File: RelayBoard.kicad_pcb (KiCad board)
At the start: 2 copper layers, 162 parts, among them P1 HE10-32, P2 CONN_2, Q1 NPN, Q10 NPN, Q11 NPN, Q12 NPN, Q13 NPN, Q14 NPN, Q15 NPN, Q16 NPN, Q17 NPN, Q18 NPN, Q19 NPN, Q2 NPN, Q20 NPN, Q21 NPN, Q22 NPN, Q23 NPN, Q24 NPN, Q25 NPN, Q26 NPN, Q27 NPN, Q28 NPN, Q29 NPN, Q3 NPN, Q30 NPN, Q31 NPN, Q32 NPN, Q4 NPN, Q5 NPN, Q6 NPN, Q7 NPN, Q8 NPN, Q9 NPN

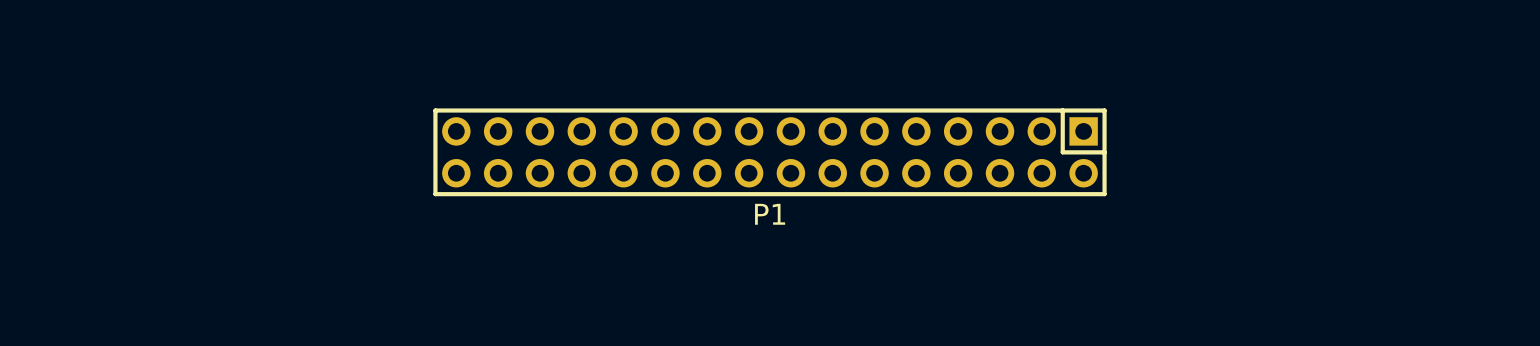
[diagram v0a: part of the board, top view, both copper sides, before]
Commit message: Changed the footprint of primary input header from 2x16 to 1x32 Due to routing concerns
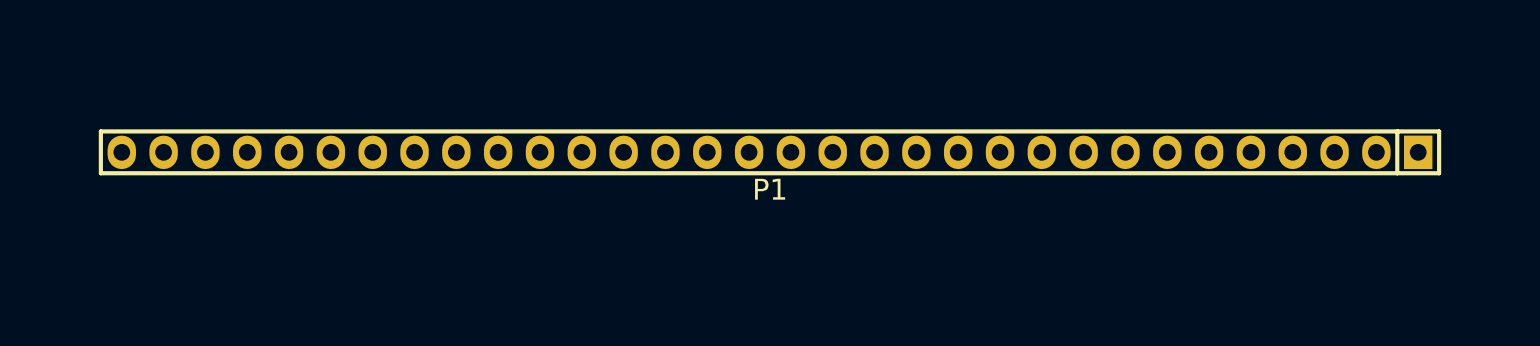
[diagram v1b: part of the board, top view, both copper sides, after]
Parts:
- P1: footprint Pin_Headers:Pin_Header_Straight_2x16 -> Pin_Headers:Pin_Header_Straight_1x32
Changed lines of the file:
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@@
     (links 320)
     (no_connects 320)
-    (area 30.48 19.05 344.17 180.34)
+    (area 30.48 20.01 343.994286 180.27)
     (thickness 1.6)
     (drawings 3)
@@
     )
   )
-  (module Pin_Headers:Pin_Header_Straight_2x16 (layer F.Cu)
+  (module Pin_Headers:Pin_Header_Straight_1x32 (layer F.Cu)
     (at 219.71 100.33 180)
     (descr "1 pin")
     (tags "CONN DEV")
-    (fp_text reference P1 (at 0 -3.81 180) (layer F.SilkS)
+    (fp_text reference P1 (at 0 -2.286 180) (layer F.SilkS)
       (effects (font (size 1.27 1.27) (thickness 0.2032)))
     )
@@
       (effects (font (size 1.27 1.27) (thickness 0.2032)))
     )
-    (fp_line (start 20.32 -2.54) (end -20.32 -2.54) (layer F.SilkS) (width 0.254))
-    (fp_line (start -17.78 2.54) (end 20.32 2.54) (layer F.SilkS) (width 0.254))
-    (fp_line (start 20.32 -2.54) (end 20.32 2.54) (layer F.SilkS) (width 0.254))
-    (fp_line (start -20.32 -2.54) (end -20.32 0) (layer F.SilkS) (width 0.254))
-    (fp_line (start -20.32 2.54) (end -17.78 2.54) (layer F.SilkS) (width 0.254))
-    (fp_line (start -20.32 0) (end -17.78 0) (layer F.SilkS) (width 0.254))
-    (fp_line (start -17.78 0) (end -17.78 2.54) (layer F.SilkS) (width 0.254))
-    (fp_line (start -20.32 2.54) (end -20.32 0) (layer F.SilkS) (width 0.254))
-    (pad 1 thru_hole rect (at -19.05 1.27 180) (size 1.7272 1.7272) (drill 1.016) (layers *.Cu *.Mask F.SilkS)
+    (fp_line (start -38.1 1.27) (end 40.64 1.27) (layer F.SilkS) (width 0.254))
+    (fp_line (start 40.64 1.27) (end 40.64 -1.27) (layer F.SilkS) (width 0.254))
+    (fp_line (start 40.64 -1.27) (end -38.1 -1.27) (layer F.SilkS) (width 0.254))
+    (fp_line (start -40.64 -1.27) (end -38.1 -1.27) (layer F.SilkS) (width 0.254))
+    (fp_line (start -38.1 -1.27) (end -38.1 1.27) (layer F.SilkS) (width 0.254))
+    (fp_line (start -40.64 -1.27) (end -40.64 1.27) (layer F.SilkS) (width 0.254))
+    (fp_line (start -40.64 1.27) (end -38.1 1.27) (layer F.SilkS) (width 0.254))
+    (pad 1 thru_hole rect (at -39.37 0 180) (size 1.7272 2.032) (drill 1.016) (layers *.Cu *.Mask F.SilkS)
       (net 1 Pin1))
-    (pad 2 thru_hole oval (at -16.51 1.27 180) (size 1.7272 1.7272) (drill 1.016) (layers *.Cu *.Mask F.SilkS)
+    (pad 2 thru_hole oval (at -36.83 0 180) (size 1.7272 2.032) (drill 1.016) (layers *.Cu *.Mask F.SilkS)
       (net 2 Pin2))
-    (pad 3 thru_hole oval (at -13.97 1.27 180) (size 1.7272 1.7272) (drill 1.016) (layers *.Cu *.Mask F.SilkS)
+    (pad 3 thru_hole oval (at -34.29 0 180) (size 1.7272 2.032) (drill 1.016) (layers *.Cu *.Mask F.SilkS)
       (net 3 Pin3))
-    (pad 4 thru_hole oval (at -11.43 1.27 180) (size 1.7272 1.7272) (drill 1.016) (layers *.Cu *.Mask F.SilkS)
+    (pad 4 thru_hole oval (at -31.75 0 180) (size 1.7272 2.032) (drill 1.016) (layers *.Cu *.Mask F.SilkS)
       (net 4 Pin4))
-    (pad 5 thru_hole oval (at -8.89 1.27 180) (size 1.7272 1.7272) (drill 1.016) (layers *.Cu *.Mask F.SilkS)
+    (pad 5 thru_hole oval (at -29.21 0 180) (size 1.7272 2.032) (drill 1.016) (layers *.Cu *.Mask F.SilkS)
       (net 5 Pin5))
-    (pad 6 thru_hole oval (at -6.35 1.27 180) (size 1.7272 1.7272) (drill 1.016) (layers *.Cu *.Mask F.SilkS)
+    (pad 6 thru_hole oval (at -26.67 0 180) (size 1.7272 2.032) (drill 1.016) (layers *.Cu *.Mask F.SilkS)
       (net 6 Pin6))
-    (pad 7 thru_hole oval (at -3.81 1.27 180) (size 1.7272 1.7272) (drill 1.016) (layers *.Cu *.Mask F.SilkS)
+    (pad 7 thru_hole oval (at -24.13 0 180) (size 1.7272 2.032) (drill 1.016) (layers *.Cu *.Mask F.SilkS)
       (net 7 Pin7))
-    (pad 8 thru_hole oval (at -1.27 1.27 180) (size 1.7272 1.7272) (drill 1.016) (layers *.Cu *.Mask F.SilkS)
+    (pad 8 thru_hole oval (at -21.59 0 180) (size 1.7272 2.032) (drill 1.016) (layers *.Cu *.Mask F.SilkS)
       (net 8 Pin8))
-    (pad 9 thru_hole oval (at 1.27 1.27 180) (size 1.7272 1.7272) (drill 1.016) (layers *.Cu *.Mask F.SilkS)
+    (pad 9 thru_hole oval (at -19.05 0 180) (size 1.7272 2.032) (drill 1.016) (layers *.Cu *.Mask F.SilkS)
       (net 9 Pin9))
-    (pad 10 thru_hole oval (at 3.81 1.27 180) (size 1.7272 1.7272) (drill 1.016) (layers *.Cu *.Mask F.SilkS)
+    (pad 10 thru_hole oval (at -16.51 0 180) (size 1.7272 2.032) (drill 1.016) (layers *.Cu *.Mask F.SilkS)
       (net 10 Pin10))
-    (pad 11 thru_hole oval (at 6.35 1.27 180) (size 1.7272 1.7272) (drill 1.016) (layers *.Cu *.Mask F.SilkS)
+    (pad 11 thru_hole oval (at -13.97 0 180) (size 1.7272 2.032) (drill 1.016) (layers *.Cu *.Mask F.SilkS)
       (net 11 Pin11))
-    (pad 12 thru_hole oval (at 8.89 1.27 180) (size 1.7272 1.7272) (drill 1.016) (layers *.Cu *.Mask F.SilkS)
+    (pad 12 thru_hole oval (at -11.43 0 180) (size 1.7272 2.032) (drill 1.016) (layers *.Cu *.Mask F.SilkS)
       (net 12 Pin12))
-    (pad 13 thru_hole oval (at 11.43 1.27 180) (size 1.7272 1.7272) (drill 1.016) (layers *.Cu *.Mask F.SilkS)
+    (pad 13 thru_hole oval (at -8.89 0 180) (size 1.7272 2.032) (drill 1.016) (layers *.Cu *.Mask F.SilkS)
       (net 13 Pin13))
-    (pad 14 thru_hole oval (at 13.97 1.27 180) (size 1.7272 1.7272) (drill 1.016) (layers *.Cu *.Mask F.SilkS)
+    (pad 14 thru_hole oval (at -6.35 0 180) (size 1.7272 2.032) (drill 1.016) (layers *.Cu *.Mask F.SilkS)
       (net 14 Pin14))
-    (pad 15 thru_hole oval (at 16.51 1.27 180) (size 1.7272 1.7272) (drill 1.016) (layers *.Cu *.Mask F.SilkS)
+    (pad 15 thru_hole oval (at -3.81 0 180) (size 1.7272 2.032) (drill 1.016) (layers *.Cu *.Mask F.SilkS)
       (net 15 Pin15))
-    (pad 16 thru_hole oval (at 19.05 1.27 180) (size 1.7272 1.7272) (drill 1.016) (layers *.Cu *.Mask F.SilkS)
+    (pad 16 thru_hole oval (at -1.27 0 180) (size 1.7272 2.032) (drill 1.016) (layers *.Cu *.Mask F.SilkS)
       (net 16 Pin16))
-    (pad 17 thru_hole oval (at 19.05 -1.27 180) (size 1.7272 1.7272) (drill 1.016) (layers *.Cu *.Mask F.SilkS)
+    (pad 17 thru_hole oval (at 1.27 0 180) (size 1.7272 2.032) (drill 1.016) (layers *.Cu *.Mask F.SilkS)
       (net 17 Pin17))
-    (pad 18 thru_hole oval (at 16.51 -1.27 180) (size 1.7272 1.7272) (drill 1.016) (layers *.Cu *.Mask F.SilkS)
+    (pad 18 thru_hole oval (at 3.81 0 180) (size 1.7272 2.032) (drill 1.016) (layers *.Cu *.Mask F.SilkS)
       (net 18 Pin18))
-    (pad 19 thru_hole oval (at 13.97 -1.27 180) (size 1.7272 1.7272) (drill 1.016) (layers *.Cu *.Mask F.SilkS)
+    (pad 19 thru_hole oval (at 6.35 0 180) (size 1.7272 2.032) (drill 1.016) (layers *.Cu *.Mask F.SilkS)
       (net 19 Pin19))
-    (pad 20 thru_hole oval (at 11.43 -1.27 180) (size 1.7272 1.7272) (drill 1.016) (layers *.Cu *.Mask F.SilkS)
+    (pad 20 thru_hole oval (at 8.89 0 180) (size 1.7272 2.032) (drill 1.016) (layers *.Cu *.Mask F.SilkS)
       (net 20 Pin20))
-    (pad 21 thru_hole oval (at 8.89 -1.27 180) (size 1.7272 1.7272) (drill 1.016) (layers *.Cu *.Mask F.SilkS)
+    (pad 21 thru_hole oval (at 11.43 0 180) (size 1.7272 2.032) (drill 1.016) (layers *.Cu *.Mask F.SilkS)
       (net 21 Pin21))
-    (pad 22 thru_hole oval (at 6.35 -1.27 180) (size 1.7272 1.7272) (drill 1.016) (layers *.Cu *.Mask F.SilkS)
+    (pad 22 thru_hole oval (at 13.97 0 180) (size 1.7272 2.032) (drill 1.016) (layers *.Cu *.Mask F.SilkS)
       (net 22 Pin22))
-    (pad 23 thru_hole oval (at 3.81 -1.27 180) (size 1.7272 1.7272) (drill 1.016) (layers *.Cu *.Mask F.SilkS)
+    (pad 23 thru_hole oval (at 16.51 0 180) (size 1.7272 2.032) (drill 1.016) (layers *.Cu *.Mask F.SilkS)
       (net 23 Pin23))
-    (pad 24 thru_hole oval (at 1.27 -1.27 180) (size 1.7272 1.7272) (drill 1.016) (layers *.Cu *.Mask F.SilkS)
+    (pad 24 thru_hole oval (at 19.05 0 180) (size 1.7272 2.032) (drill 1.016) (layers *.Cu *.Mask F.SilkS)
       (net 24 Pin24))
-    (pad 25 thru_hole oval (at -1.27 -1.27 180) (size 1.7272 1.7272) (drill 1.016) (layers *.Cu *.Mask F.SilkS)
+    (pad 25 thru_hole oval (at 21.59 0 180) (size 1.7272 2.032) (drill 1.016) (layers *.Cu *.Mask F.SilkS)
       (net 25 Pin25))
-    (pad 26 thru_hole oval (at -3.81 -1.27 180) (size 1.7272 1.7272) (drill 1.016) (layers *.Cu *.Mask F.SilkS)
+    (pad 26 thru_hole oval (at 24.13 0 180) (size 1.7272 2.032) (drill 1.016) (layers *.Cu *.Mask F.SilkS)
       (net 26 Pin26))
-    (pad 27 thru_hole oval (at -6.35 -1.27 180) (size 1.7272 1.7272) (drill 1.016) (layers *.Cu *.Mask F.SilkS)
+    (pad 27 thru_hole oval (at 26.67 0 180) (size 1.7272 2.032) (drill 1.016) (layers *.Cu *.Mask F.SilkS)
       (net 27 Pin27))
-    (pad 28 thru_hole oval (at -8.89 -1.27 180) (size 1.7272 1.7272) (drill 1.016) (layers *.Cu *.Mask F.SilkS)
+    (pad 28 thru_hole oval (at 29.21 0 180) (size 1.7272 2.032) (drill 1.016) (layers *.Cu *.Mask F.SilkS)
       (net 28 Pin28))
-    (pad 29 thru_hole oval (at -11.43 -1.27 180) (size 1.7272 1.7272) (drill 1.016) (layers *.Cu *.Mask F.SilkS)
+    (pad 29 thru_hole oval (at 31.75 0 180) (size 1.7272 2.032) (drill 1.016) (layers *.Cu *.Mask F.SilkS)
       (net 29 Pin29))
-    (pad 30 thru_hole oval (at -13.97 -1.27 180) (size 1.7272 1.7272) (drill 1.016) (layers *.Cu *.Mask F.SilkS)
+    (pad 30 thru_hole oval (at 34.29 0 180) (size 1.7272 2.032) (drill 1.016) (layers *.Cu *.Mask F.SilkS)
       (net 30 Pin30))
-    (pad 31 thru_hole oval (at -16.51 -1.27 180) (size 1.7272 1.7272) (drill 1.016) (layers *.Cu *.Mask F.SilkS)
+    (pad 31 thru_hole oval (at 36.83 0 180) (size 1.7272 2.032) (drill 1.016) (layers *.Cu *.Mask F.SilkS)
       (net 31 Pin31))
-    (pad 32 thru_hole oval (at -19.05 -1.27 180) (size 1.7272 1.7272) (drill 1.016) (layers *.Cu *.Mask F.SilkS)
+    (pad 32 thru_hole oval (at 39.37 0 180) (size 1.7272 2.032) (drill 1.016) (layers *.Cu *.Mask F.SilkS)
       (net 32 Pin32))
-    (model Pin_Headers/Pin_Header_Straight_2x16.wrl
+    (model Pin_Headers/Pin_Header_Straight_1x32.wrl
       (at (xyz 0 0 0))
       (scale (xyz 1 1 1))

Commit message: Just finished routing
Autoroute is amazing!
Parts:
- moved RE10 4.45 mm to (134.6, 141.6)
- moved RE12 4.45 mm to (151.1, 141.6)
- moved RE14 4.45 mm to (167.6, 141.6)
- moved RE16 4.45 mm to (184.2, 141.6)
- moved RE18 4.45 mm to (200.7, 141.6)
- moved RE2 4.45 mm to (68.6, 141.6)
- moved RE20 4.45 mm to (217.2, 141.6)
- moved RE22 4.45 mm to (233.7, 141.6)
- moved RE24 4.45 mm to (250.2, 141.6)
- moved RE26 4.45 mm to (266.7, 141.6)
- moved RE28 4.45 mm to (283.2, 141.6)
- moved RE30 4.45 mm to (299.7, 141.6)
- moved RE32 4.45 mm to (316.2, 141.6)
- moved RE4 4.45 mm to (85.1, 141.6)
- moved RE6 4.45 mm to (101.6, 141.6)
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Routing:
- net +5V: track 0.00 -> 844.2 mm, vias 0 -> 2
- net GND: track 0.00 -> 601.2 mm
- net Pin1: track 0.00 -> 231.3 mm, vias 0 -> 3
- net Pin2: track 0.00 -> 208.5 mm, vias 0 -> 4
- net Pin3: track 0.00 -> 189.3 mm, vias 0 -> 4
- net Pin32: track 0.00 -> 172.8 mm, vias 0 -> 4
- net Pin4: track 0.00 -> 163.0 mm, vias 0 -> 4
- net Pin17: track 0.00 -> 154.7 mm, vias 0 -> 1
- net Pin31: track 0.00 -> 147.9 mm, vias 0 -> 2
- net Pin18: track 0.00 -> 142.2 mm, vias 0 -> 1
- net Pin5: track 0.00 -> 139.4 mm, vias 0 -> 3
- net Pin30: track 0.00 -> 124.0 mm, vias 0 -> 4
- net Pin19: track 0.00 -> 122.3 mm, vias 0 -> 2
- net Pin6: track 0.00 -> 119.3 mm, vias 0 -> 3
- net Pin16: track 0.00 -> 111.6 mm, vias 0 -> 2
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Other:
- rule trace_min: 0.254 -> 0.95

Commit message: Stuff
* Dimension Drawing
* PCB Edges are now included
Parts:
- moved D13 30.5 mm to (143.5, 54.0)
- moved D16 30.5 mm to (161.3, 145.4)
- moved D19 30.5 mm to (193.0, 54.0)
- moved D22 30.5 mm to (210.8, 145.4)
- moved D23 30.5 mm to (226.1, 54.0)
- moved D25 30.5 mm to (242.6, 54.0)
- moved D27 30.5 mm to (259.1, 54.0)
- moved D29 30.5 mm to (275.6, 54.0)
- moved D32 30.5 mm to (293.4, 145.4)
- moved P1 30.5 mm to (189.2, 101.6)
- moved Q13 30.5 mm to (147.3, 83.2)
- moved Q14 30.5 mm to (147.3, 117.5)
- moved Q19 30.5 mm to (196.8, 83.2)
- moved Q20 30.5 mm to (196.8, 117.5)
- moved Q21 30.5 mm to (214.6, 83.2)
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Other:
- board outline added: 271.8 x 106.7 mm
- board text removed: "Board is 217mm x 118mm"
